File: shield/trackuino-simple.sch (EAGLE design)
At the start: 11 parts, among them T1 BC547, U1 ARDUINO_SHIELDNOHOLES

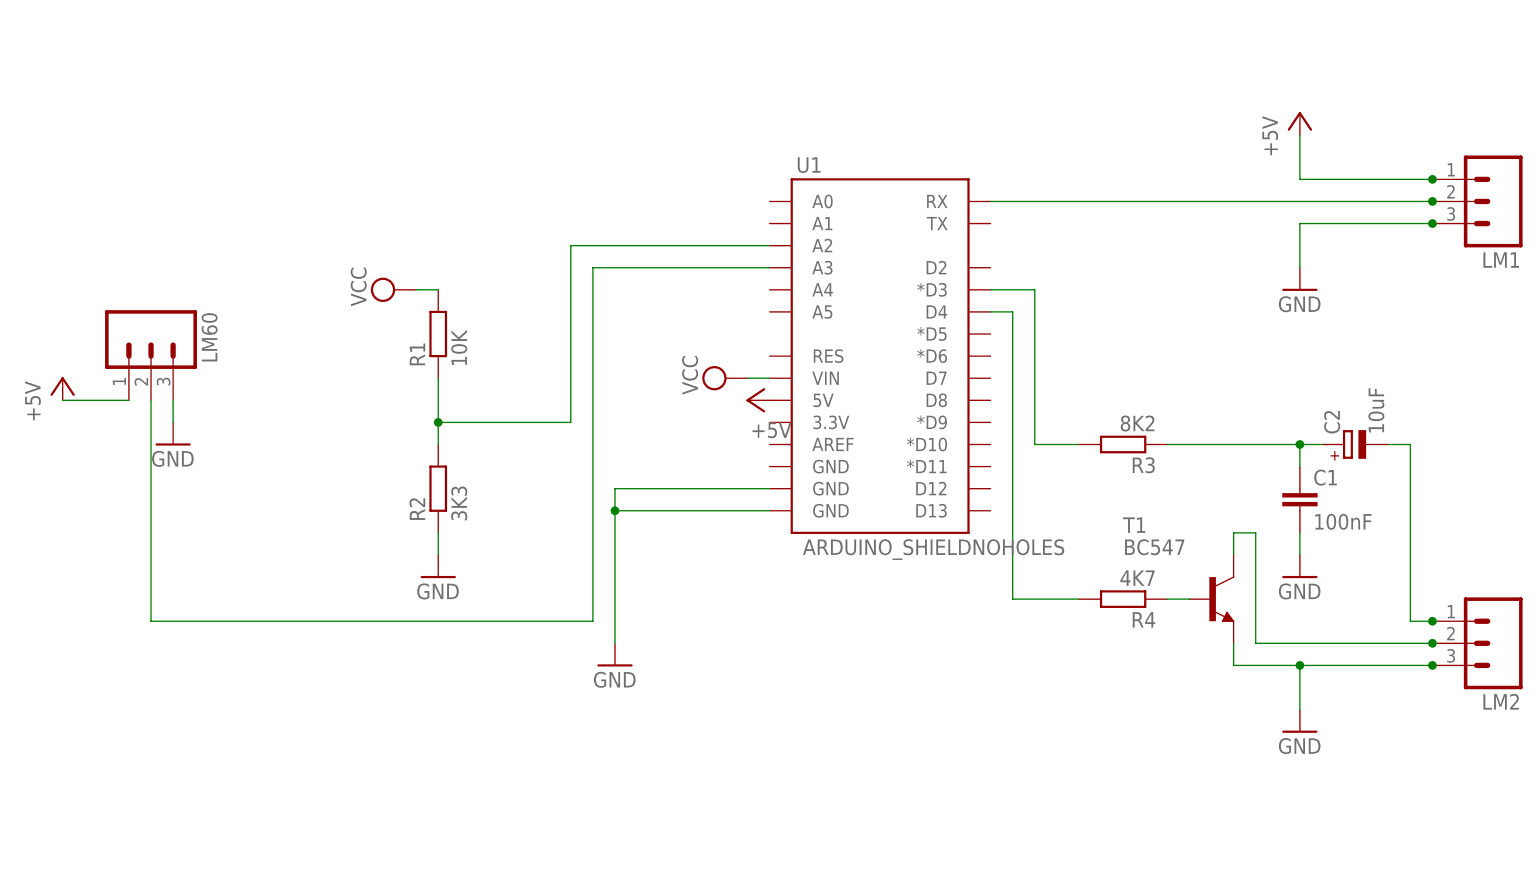
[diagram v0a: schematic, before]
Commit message: Serial GPS support for shield
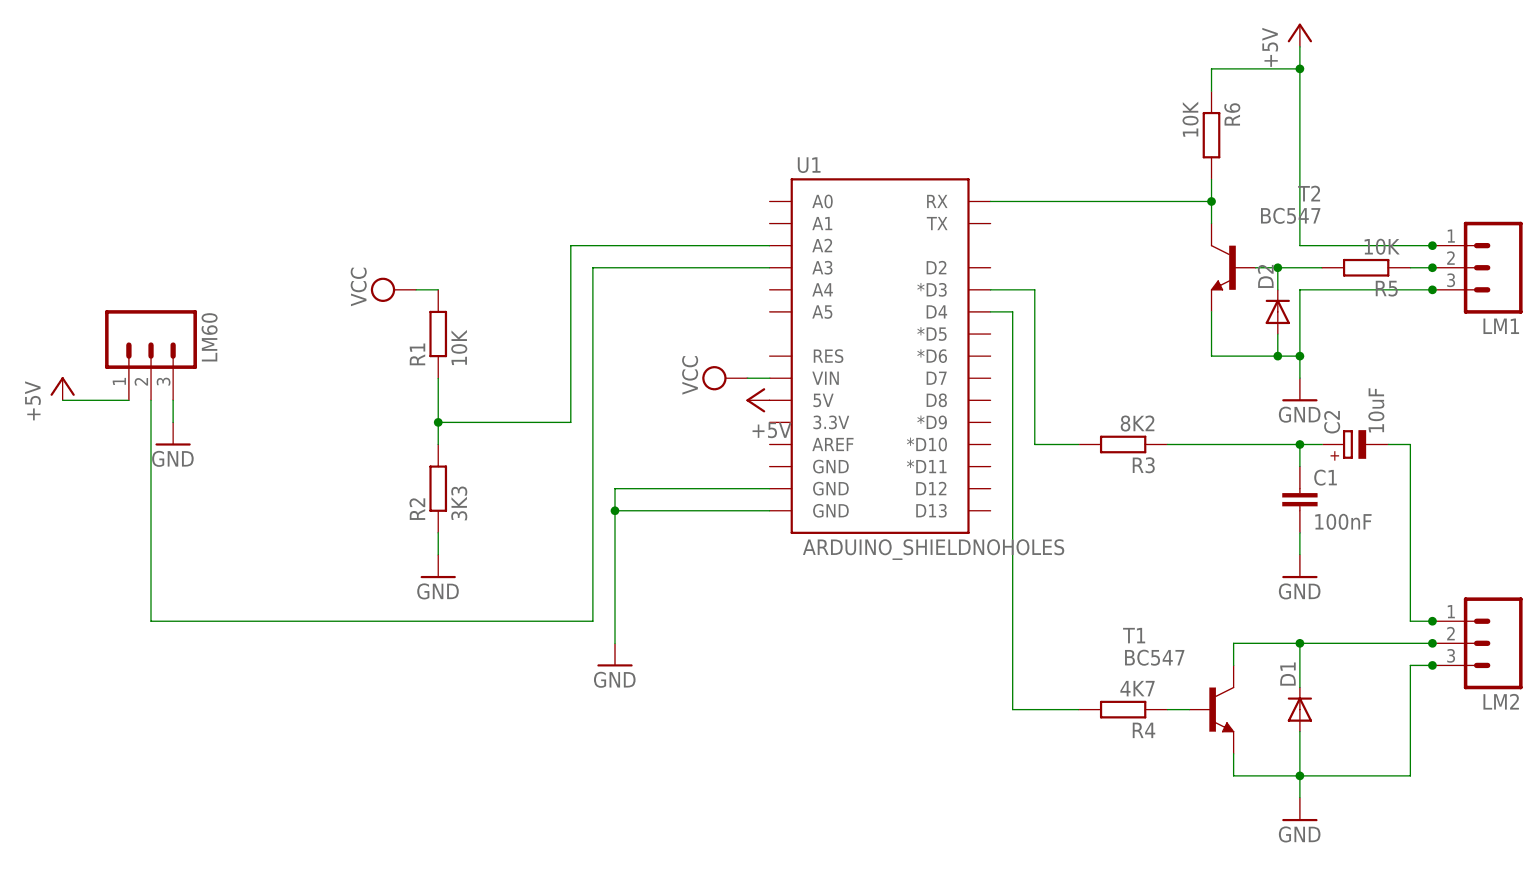
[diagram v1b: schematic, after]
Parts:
- added D1, D2: (no value), diode:DIODE-DO41-10
- added R5, R6: 10K, resistor:R-EU_0207/10
- added T2: BC547, transistor:BC547
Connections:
- new net N$10: LM1.2, R5.1
- new net N$5: D2.C, R5.2, T2.B
- net +5V: now also R6.1
- net GND: now also D1.A, D2.A, T2.E
- net N$1: now also R6.2, T2.C; no longer LM1.2
- net N$7: now also D1.C
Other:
- moved on the sheet: LM1, R4, T1
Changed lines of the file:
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@@
 <part name="C1" library="resistor" deviceset="C-EU" device="050-025X075" value="100nF"/>
 <part name="C2" library="resistor" deviceset="CPOL-EU" device="E2.5-6" value="10uF"/>
+<part name="T2" library="transistor" deviceset="BC547" device=""/>
+<part name="R5" library="resistor" deviceset="R-EU_" device="0207/10" value="10K"/>
+<part name="R6" library="resistor" deviceset="R-EU_" device="0207/10" value="10K"/>
+<part name="D1" library="diode" deviceset="DIODE-" device="DO41-10"/>
+<part name="D2" library="diode" deviceset="DIODE-" device="DO41-10"/>
 </parts>
 <sheets>
@@
 <instance part="U1" gate="G$1" x="116.84" y="93.98"/>
 <instance part="GND1" gate="1" x="86.36" y="58.42"/>
-<instance part="GND5" gate="1" x="165.1" y="101.6"/>
+<instance part="GND5" gate="1" x="165.1" y="88.9"/>
 <instance part="R1" gate="G$1" x="66.04" y="96.52" rot="R90"/>
 <instance part="R2" gate="G$1" x="66.04" y="78.74" rot="R90"/>
@@
 <instance part="P+4" gate="1" x="22.86" y="91.44"/>
 <instance part="P+1" gate="1" x="101.6" y="88.9" rot="R90"/>
-<instance part="P+5" gate="1" x="165.1" y="121.92"/>
+<instance part="P+5" gate="1" x="165.1" y="132.08"/>
 <instance part="GND2" gate="1" x="165.1" y="68.58"/>
 <instance part="LM60" gate="G$1" x="33.02" y="96.52" rot="R270"/>
-<instance part="LM1" gate="G$1" x="187.96" y="111.76" rot="R180"/>
-<instance part="R4" gate="G$1" x="144.78" y="66.04" rot="R180"/>
-<instance part="T1" gate="G$1" x="154.94" y="66.04"/>
+<instance part="LM1" gate="G$1" x="187.96" y="104.14" rot="R180"/>
+<instance part="R4" gate="G$1" x="144.78" y="53.34" rot="R180"/>
+<instance part="T1" gate="G$1" x="154.94" y="53.34"/>
 <instance part="LM2" gate="G$1" x="187.96" y="60.96" rot="R180"/>
-<instance part="GND3" gate="1" x="165.1" y="50.8"/>
+<instance part="GND3" gate="1" x="165.1" y="40.64"/>
 <instance part="R3" gate="G$1" x="144.78" y="83.82" rot="R180"/>
 <instance part="C1" gate="G$1" x="165.1" y="78.74"/>
 <instance part="C2" gate="G$1" x="170.18" y="83.82" rot="R90"/>
+<instance part="T2" gate="G$1" x="157.48" y="104.14" rot="MR0"/>
+<instance part="R5" gate="G$1" x="172.72" y="104.14" rot="R180"/>
+<instance part="R6" gate="G$1" x="154.94" y="119.38" rot="R270"/>
+<instance part="D1" gate="G$1" x="165.1" y="53.34" rot="R90"/>
+<instance part="D2" gate="G$1" x="162.56" y="99.06" rot="R90"/>
 </instances>
 <busses>
@@
 <segment>
 <pinref part="GND5" gate="1" pin="GND"/>
-<wire x1="165.1" y1="104.14" x2="165.1" y2="109.22" width="0.1524" layer="91"/>
-<wire x1="165.1" y1="109.22" x2="180.34" y2="109.22" width="0.1524" layer="91"/>
+<wire x1="165.1" y1="91.44" x2="165.1" y2="93.98" width="0.1524" layer="91"/>
+<wire x1="165.1" y1="93.98" x2="165.1" y2="101.6" width="0.1524" layer="91"/>
+<wire x1="165.1" y1="101.6" x2="180.34" y2="101.6" width="0.1524" layer="91"/>
 <pinref part="LM1" gate="G$1" pin="3"/>
-<junction x="180.34" y="109.22"/>
-</segment>
-<segment>
-<pinref part="LM2" gate="G$1" pin="3"/>
-<pinref part="GND3" gate="1" pin="GND"/>
-<wire x1="180.34" y1="58.42" x2="165.1" y2="58.42" width="0.1524" layer="91"/>
-<wire x1="165.1" y1="58.42" x2="165.1" y2="53.34" width="0.1524" layer="91"/>
-<pinref part="T1" gate="G$1" pin="E"/>
-<wire x1="157.48" y1="60.96" x2="157.48" y2="58.42" width="0.1524" layer="91"/>
-<wire x1="157.48" y1="58.42" x2="165.1" y2="58.42" width="0.1524" layer="91"/>
-<junction x="165.1" y="58.42"/>
-<junction x="180.34" y="58.42"/>
+<junction x="180.34" y="101.6"/>
+<pinref part="D2" gate="G$1" pin="A"/>
+<wire x1="162.56" y1="96.52" x2="162.56" y2="93.98" width="0.1524" layer="91"/>
+<wire x1="162.56" y1="93.98" x2="165.1" y2="93.98" width="0.1524" layer="91"/>
+<pinref part="T2" gate="G$1" pin="E"/>
+<wire x1="154.94" y1="99.06" x2="154.94" y2="93.98" width="0.1524" layer="91"/>
+<wire x1="154.94" y1="93.98" x2="162.56" y2="93.98" width="0.1524" layer="91"/>
+<junction x="162.56" y="93.98"/>
+<junction x="165.1" y="93.98"/>
 </segment>
 <segment>
@@
 <wire x1="35.56" y1="88.9" x2="35.56" y2="86.36" width="0.1524" layer="91"/>
 </segment>
+<segment>
+<pinref part="T1" gate="G$1" pin="E"/>
+<wire x1="157.48" y1="48.26" x2="157.48" y2="45.72" width="0.1524" layer="91"/>
+<wire x1="157.48" y1="45.72" x2="165.1" y2="45.72" width="0.1524" layer="91"/>
+<wire x1="165.1" y1="45.72" x2="177.8" y2="45.72" width="0.1524" layer="91"/>
+<wire x1="177.8" y1="45.72" x2="177.8" y2="58.42" width="0.1524" layer="91"/>
+<pinref part="LM2" gate="G$1" pin="3"/>
+<wire x1="177.8" y1="58.42" x2="180.34" y2="58.42" width="0.1524" layer="91"/>
+<pinref part="GND3" gate="1" pin="GND"/>
+<wire x1="165.1" y1="45.72" x2="165.1" y2="43.18" width="0.1524" layer="91"/>
+<pinref part="D1" gate="G$1" pin="A"/>
+<wire x1="165.1" y1="50.8" x2="165.1" y2="45.72" width="0.1524" layer="91"/>
+<junction x="165.1" y="45.72"/>
+<junction x="180.34" y="58.42"/>
+</segment>
 </net>
 <net name="+5V" class="0">
@@
 <segment>
 <pinref part="P+5" gate="1" pin="+5V"/>
-<wire x1="165.1" y1="119.38" x2="165.1" y2="114.3" width="0.1524" layer="91"/>
-<wire x1="165.1" y1="114.3" x2="180.34" y2="114.3" width="0.1524" layer="91"/>
+<wire x1="165.1" y1="129.54" x2="165.1" y2="127" width="0.1524" layer="91"/>
+<wire x1="165.1" y1="127" x2="165.1" y2="106.68" width="0.1524" layer="91"/>
+<wire x1="165.1" y1="106.68" x2="180.34" y2="106.68" width="0.1524" layer="91"/>
 <pinref part="LM1" gate="G$1" pin="1"/>
-<junction x="180.34" y="114.3"/>
+<junction x="180.34" y="106.68"/>
+<pinref part="R6" gate="G$1" pin="1"/>
+<wire x1="154.94" y1="124.46" x2="154.94" y2="127" width="0.1524" layer="91"/>
+<wire x1="154.94" y1="127" x2="165.1" y2="127" width="0.1524" layer="91"/>
+<junction x="165.1" y="127"/>
 </segment>
 </net>
@@
 <net name="N$3" class="0">
 <segment>
-<wire x1="132.08" y1="99.06" x2="132.08" y2="66.04" width="0.1524" layer="91"/>
+<wire x1="132.08" y1="99.06" x2="132.08" y2="53.34" width="0.1524" layer="91"/>
 <pinref part="R4" gate="G$1" pin="2"/>
-<wire x1="132.08" y1="66.04" x2="139.7" y2="66.04" width="0.1524" layer="91"/>
+<wire x1="132.08" y1="53.34" x2="139.7" y2="53.34" width="0.1524" layer="91"/>
 <pinref part="U1" gate="G$1" pin="D4"/>
 <wire x1="129.54" y1="99.06" x2="132.08" y2="99.06" width="0.1524" layer="91"/>
@@
 <pinref part="R4" gate="G$1" pin="1"/>
 <pinref part="T1" gate="G$1" pin="B"/>
-<wire x1="149.86" y1="66.04" x2="152.4" y2="66.04" width="0.1524" layer="91"/>
-</segment>
-</net>
-<net name="N$7" class="0">
-<segment>
-<pinref part="T1" gate="G$1" pin="C"/>
-<wire x1="157.48" y1="71.12" x2="157.48" y2="73.66" width="0.1524" layer="91"/>
-<wire x1="157.48" y1="73.66" x2="160.02" y2="73.66" width="0.1524" layer="91"/>
-<wire x1="160.02" y1="73.66" x2="160.02" y2="60.96" width="0.1524" layer="91"/>
-<pinref part="LM2" gate="G$1" pin="2"/>
-<wire x1="160.02" y1="60.96" x2="180.34" y2="60.96" width="0.1524" layer="91"/>
-<junction x="180.34" y="60.96"/>
+<wire x1="149.86" y1="53.34" x2="152.4" y2="53.34" width="0.1524" layer="91"/>
 </segment>
 </net>
@@
 <net name="N$1" class="0">
 <segment>
+<pinref part="R6" gate="G$1" pin="2"/>
+<pinref part="T2" gate="G$1" pin="C"/>
+<wire x1="154.94" y1="114.3" x2="154.94" y2="111.76" width="0.1524" layer="91"/>
 <pinref part="U1" gate="G$1" pin="RX"/>
+<wire x1="154.94" y1="111.76" x2="154.94" y2="109.22" width="0.1524" layer="91"/>
+<wire x1="129.54" y1="111.76" x2="154.94" y2="111.76" width="0.1524" layer="91"/>
+<junction x="154.94" y="111.76"/>
+</segment>
+</net>
+<net name="N$5" class="0">
+<segment>
+<pinref part="T2" gate="G$1" pin="B"/>
+<pinref part="R5" gate="G$1" pin="2"/>
+<wire x1="160.02" y1="104.14" x2="162.56" y2="104.14" width="0.1524" layer="91"/>
+<pinref part="D2" gate="G$1" pin="C"/>
+<wire x1="162.56" y1="104.14" x2="167.64" y2="104.14" width="0.1524" layer="91"/>
+<wire x1="162.56" y1="104.14" x2="162.56" y2="101.6" width="0.1524" layer="91"/>
+<junction x="162.56" y="104.14"/>
+</segment>
+</net>
+<net name="N$10" class="0">
+<segment>
+<pinref part="R5" gate="G$1" pin="1"/>
 <pinref part="LM1" gate="G$1" pin="2"/>
-<wire x1="129.54" y1="111.76" x2="180.34" y2="111.76" width="0.1524" layer="91"/>
-<junction x="180.34" y="111.76"/>
-</segment>
-</net>
+<wire x1="177.8" y1="104.14" x2="180.34" y2="104.14" width="0.1524" layer="91"/>
+<junction x="180.34" y="104.14"/>
+</segment>
+</net>
+<net name="N$7" class="0">
+<segment>
+<pinref part="T1" gate="G$1" pin="C"/>
+<wire x1="157.48" y1="58.42" x2="157.48" y2="60.96" width="0.1524" layer="91"/>
+<pinref part="LM2" gate="G$1" pin="2"/>
+<wire x1="157.48" y1="60.96" x2="165.1" y2="60.96" width="0.1524" layer="91"/>
+<pinref part="D1" gate="G$1" pin="C"/>
+<wire x1="165.1" y1="60.96" x2="180.34" y2="60.96" width="0.1524" layer="91"/>
+<wire x1="165.1" y1="60.96" x2="165.1" y2="55.88" width="0.1524" layer="91"/>
+<junction x="165.1" y="60.96"/>
+<junction x="180.34" y="60.96"/>
+</segment>
+</net>

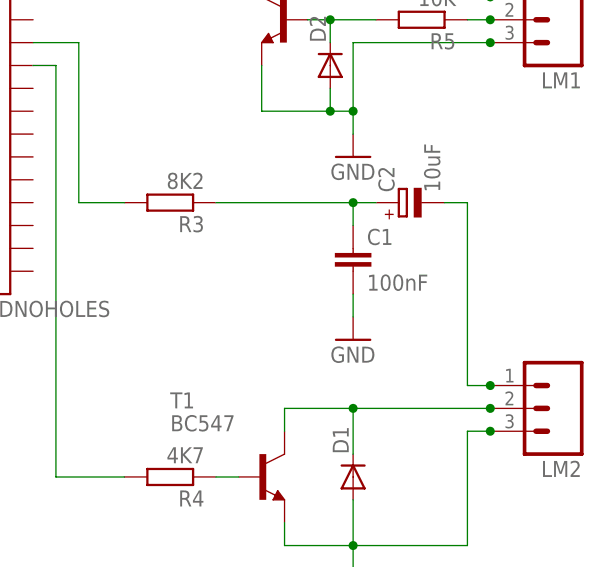
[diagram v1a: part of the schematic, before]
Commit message: Change output filter capacitor value
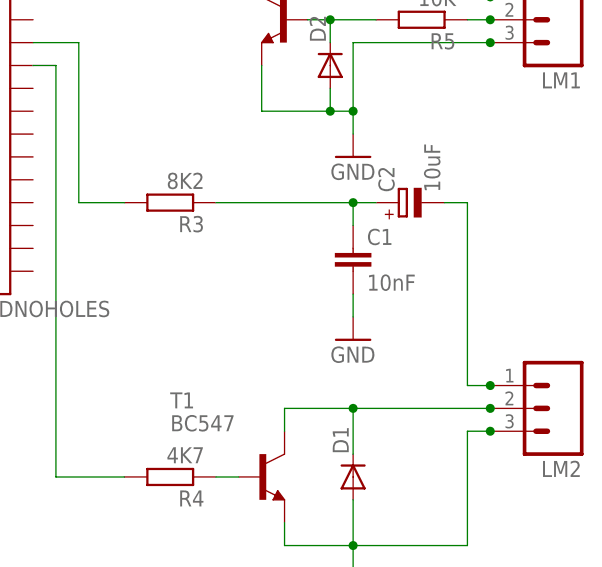
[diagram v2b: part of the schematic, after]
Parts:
- C1: value 100nF -> 10nF
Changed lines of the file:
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@@
 <part name="GND3" library="supply1" deviceset="GND" device=""/>
 <part name="R3" library="rcl" deviceset="R-EU_" device="0207/10" value="8K2"/>
-<part name="C1" library="resistor" deviceset="C-EU" device="050-025X075" value="100nF"/>
+<part name="C1" library="resistor" deviceset="C-EU" device="050-025X075" value="10nF"/>
 <part name="C2" library="resistor" deviceset="CPOL-EU" device="E2.5-6" value="10uF"/>
 <part name="T2" library="transistor" deviceset="BC547" device=""/>
